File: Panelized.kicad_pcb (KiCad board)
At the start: 2 copper layers, 54.9 x 18.3 mm, 88 parts, among them J1 Conn_01x01_Pin, J2 Conn_01x01_Pin, J3 Conn_01x01_Pin, J4 Conn_01x01_Pin, Q1 AO3400A, Q2 AO3401A, U1 LM393

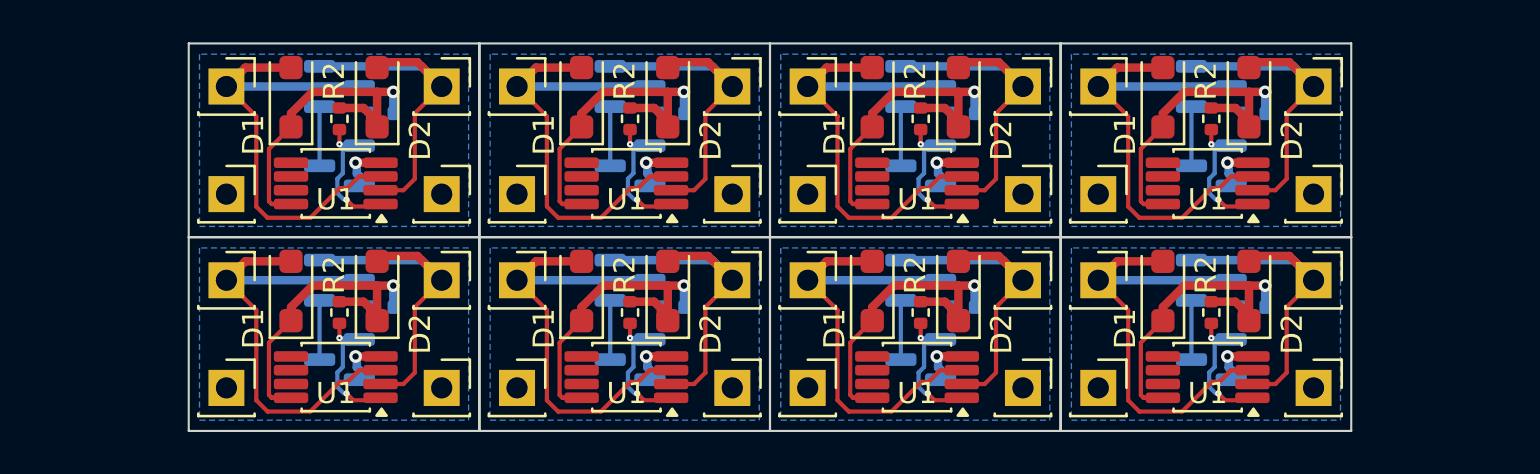
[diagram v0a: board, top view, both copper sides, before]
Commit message: Fixed wrong footprint issue
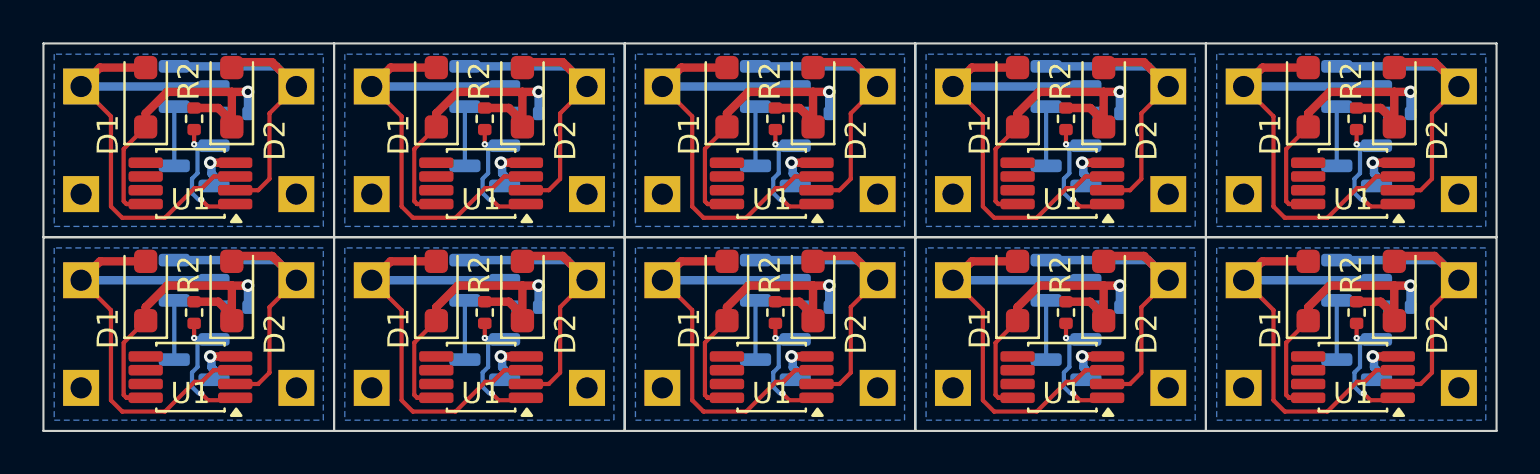
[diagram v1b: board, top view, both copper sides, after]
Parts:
- removed the D1 at (125.9, 31.7)
- removed the D1 at (139.6, 22.5)
- removed the D1 at (125.9, 22.5)
- removed the D1 at (167.0, 31.7)
- removed the D1 at (139.6, 31.7)
- removed the D1 at (167.0, 22.5)
- removed the D1 at (153.3, 22.5)
- removed the D1 at (153.3, 31.7)
- removed the D2 at (143.7, 31.7)
- removed the D2 at (171.1, 22.5)
- removed the D2 at (130.0, 31.7)
- removed the D2 at (157.4, 22.5)
- removed the D2 at (157.4, 31.7)
- removed the D2 at (130.0, 22.5)
- removed the D2 at (171.1, 31.7)
- removed the D2 at (143.7, 22.5)
- removed the J1 at (150.3, 22.0)
- removed the J1 at (164.0, 22.0)
- removed the J1 at (164.0, 31.2)
- removed the J1 at (122.8, 31.2)
- removed the J1 at (150.3, 31.2)
- removed the J1 at (136.6, 22.0)
- removed the J1 at (136.6, 31.2)
- removed the J1 at (122.8, 22.0)
- removed the J2 at (164.0, 27.1)
- removed the J2 at (150.3, 36.3)
- removed the J2 at (136.6, 27.1)
- removed the J2 at (150.3, 27.1)
- removed the J2 at (136.6, 36.3)
- removed the J2 at (122.8, 27.1)
- removed the J2 at (164.0, 36.3)
- removed the J2 at (122.8, 36.3)
- removed the J3 at (174.2, 31.2)
- removed the J3 at (174.2, 22.0)
- removed the J3 at (146.7, 22.0)
- removed the J3 at (133.0, 31.2)
- removed the J3 at (160.4, 31.2)
- removed the J3 at (146.7, 31.2)
- removed the J3 at (133.0, 22.0)
- removed the J3 at (160.4, 22.0)
- removed the J4 at (146.7, 27.1)
- removed the J4 at (160.4, 36.3)
- removed the J4 at (133.0, 27.1)
- removed the J4 at (133.0, 36.3)
- removed the J4 at (146.7, 36.3)
- removed the J4 at (174.2, 36.3)
- removed the J4 at (160.4, 27.1)
- removed the J4 at (174.2, 27.1)
- removed the Q1 at (128.2, 34.9)
- removed the Q1 at (128.2, 25.8)
- removed the Q1 at (155.6, 34.9)
- removed the Q1 at (169.3, 34.9)
- removed the Q1 at (141.9, 25.8)
- removed the Q1 at (155.6, 25.8)
- removed the Q1 at (141.9, 34.9)
- removed the Q1 at (169.3, 25.8)
- removed the Q2 at (169.3, 31.2)
- removed the Q2 at (155.6, 31.2)
- removed the Q2 at (141.9, 31.2)
- removed the Q2 at (128.2, 22.0)
- removed the Q2 at (169.3, 22.0)
- removed the Q2 at (141.9, 22.0)
- removed the Q2 at (155.6, 22.0)
- removed the Q2 at (128.2, 31.2)
- removed the R1 at (143.9, 23.3)
- removed the R1 at (157.6, 32.4)
- removed the R1 at (143.9, 32.4)
- removed the R1 at (130.2, 32.4)
- removed the R1 at (171.4, 32.4)
- removed the R1 at (130.2, 23.3)
- removed the R1 at (171.4, 23.3)
- removed the R1 at (157.6, 23.3)
- removed the R2 at (155.6, 32.7)
- removed the R2 at (128.2, 23.6)
- removed the R2 at (141.9, 32.7)
- removed the R2 at (169.3, 32.7)
- removed the R2 at (155.6, 23.6)
- removed the R2 at (169.3, 23.6)
- removed the R2 at (141.9, 23.6)
- removed the R2 at (128.2, 32.7)
- removed the U1 at (128.0, 35.7)
- removed the U1 at (141.7, 26.6)
- removed the U1 at (128.0, 26.6)
- removed the U1 at (169.2, 35.7)
- removed the U1 at (169.2, 26.6)
- removed the U1 at (155.4, 26.6)
- removed the U1 at (141.7, 35.7)
- removed the U1 at (155.4, 35.7)
- added D1: PMEG2020EH, Diode_SMD:D_SOD-123F, F.Cu at (160.2, 22.5)
- added D1: PMEG2020EH, Diode_SMD:D_SOD-123F, F.Cu at (119.0, 22.5)
- added D1: PMEG2020EH, Diode_SMD:D_SOD-123F, F.Cu at (146.5, 22.5)
- added D1: PMEG2020EH, Diode_SMD:D_SOD-123F, F.Cu at (173.9, 22.5)
- added D1: PMEG2020EH, Diode_SMD:D_SOD-123F, F.Cu at (173.9, 31.7)
- added D1: PMEG2020EH, Diode_SMD:D_SOD-123F, F.Cu at (132.8, 22.5)
- added D1: PMEG2020EH, Diode_SMD:D_SOD-123F, F.Cu at (146.5, 31.7)
- added D1: PMEG2020EH, Diode_SMD:D_SOD-123F, F.Cu at (132.8, 31.7)
- added D1: PMEG2020EH, Diode_SMD:D_SOD-123F, F.Cu at (119.0, 31.7)
- added D1: PMEG2020EH, Diode_SMD:D_SOD-123F, F.Cu at (160.2, 31.7)
- added D2: PMEG2020EH, Diode_SMD:D_SOD-123F, F.Cu at (178.0, 22.5)
- added D2: PMEG2020EH, Diode_SMD:D_SOD-123F, F.Cu at (150.5, 22.5)
- added D2: PMEG2020EH, Diode_SMD:D_SOD-123F, F.Cu at (178.0, 31.7)
- added D2: PMEG2020EH, Diode_SMD:D_SOD-123F, F.Cu at (136.8, 22.5)
- added D2: PMEG2020EH, Diode_SMD:D_SOD-123F, F.Cu at (164.2, 22.5)
- added D2: PMEG2020EH, Diode_SMD:D_SOD-123F, F.Cu at (136.8, 31.7)
- added D2: PMEG2020EH, Diode_SMD:D_SOD-123F, F.Cu at (150.5, 31.7)
- added D2: PMEG2020EH, Diode_SMD:D_SOD-123F, F.Cu at (123.1, 22.5)
- added D2: PMEG2020EH, Diode_SMD:D_SOD-123F, F.Cu at (164.2, 31.7)
- added D2: PMEG2020EH, Diode_SMD:D_SOD-123F, F.Cu at (123.1, 31.7)
- added J1: Conn_01x01_Pin, Connector_PinHeader_2.54mm:PinHeader_1x01_P2.54mm_Vertical, B.Cu at (170.9, 22.0)
- added J1: Conn_01x01_Pin, Connector_PinHeader_2.54mm:PinHeader_1x01_P2.54mm_Vertical, B.Cu at (157.1, 31.2)
- added J1: Conn_01x01_Pin, Connector_PinHeader_2.54mm:PinHeader_1x01_P2.54mm_Vertical, B.Cu at (116.0, 22.0)
- added J1: Conn_01x01_Pin, Connector_PinHeader_2.54mm:PinHeader_1x01_P2.54mm_Vertical, B.Cu at (157.1, 22.0)
- added J1: Conn_01x01_Pin, Connector_PinHeader_2.54mm:PinHeader_1x01_P2.54mm_Vertical, B.Cu at (129.7, 22.0)
- added J1: Conn_01x01_Pin, Connector_PinHeader_2.54mm:PinHeader_1x01_P2.54mm_Vertical, B.Cu at (129.7, 31.2)
- added J1: Conn_01x01_Pin, Connector_PinHeader_2.54mm:PinHeader_1x01_P2.54mm_Vertical, B.Cu at (143.4, 22.0)
- added J1: Conn_01x01_Pin, Connector_PinHeader_2.54mm:PinHeader_1x01_P2.54mm_Vertical, B.Cu at (116.0, 31.2)
- added J1: Conn_01x01_Pin, Connector_PinHeader_2.54mm:PinHeader_1x01_P2.54mm_Vertical, B.Cu at (143.4, 31.2)
- added J1: Conn_01x01_Pin, Connector_PinHeader_2.54mm:PinHeader_1x01_P2.54mm_Vertical, B.Cu at (170.9, 31.2)
- added J2: Conn_01x01_Pin, Connector_PinHeader_2.54mm:PinHeader_1x01_P2.54mm_Vertical, B.Cu at (129.7, 27.1)
- added J2: Conn_01x01_Pin, Connector_PinHeader_2.54mm:PinHeader_1x01_P2.54mm_Vertical, B.Cu at (157.1, 36.3)
- added J2: Conn_01x01_Pin, Connector_PinHeader_2.54mm:PinHeader_1x01_P2.54mm_Vertical, B.Cu at (143.4, 27.1)
- added J2: Conn_01x01_Pin, Connector_PinHeader_2.54mm:PinHeader_1x01_P2.54mm_Vertical, B.Cu at (157.1, 27.1)
- added J2: Conn_01x01_Pin, Connector_PinHeader_2.54mm:PinHeader_1x01_P2.54mm_Vertical, B.Cu at (116.0, 36.3)
- added J2: Conn_01x01_Pin, Connector_PinHeader_2.54mm:PinHeader_1x01_P2.54mm_Vertical, B.Cu at (116.0, 27.1)
- added J2: Conn_01x01_Pin, Connector_PinHeader_2.54mm:PinHeader_1x01_P2.54mm_Vertical, B.Cu at (143.4, 36.3)
- added J2: Conn_01x01_Pin, Connector_PinHeader_2.54mm:PinHeader_1x01_P2.54mm_Vertical, B.Cu at (129.7, 36.3)
- added J2: Conn_01x01_Pin, Connector_PinHeader_2.54mm:PinHeader_1x01_P2.54mm_Vertical, B.Cu at (170.9, 36.3)
- added J2: Conn_01x01_Pin, Connector_PinHeader_2.54mm:PinHeader_1x01_P2.54mm_Vertical, B.Cu at (170.9, 27.1)
- added J3: Conn_01x01_Pin, Connector_PinHeader_2.54mm:PinHeader_1x01_P2.54mm_Vertical, B.Cu at (139.9, 22.0)
- added J3: Conn_01x01_Pin, Connector_PinHeader_2.54mm:PinHeader_1x01_P2.54mm_Vertical, B.Cu at (181.0, 22.0)
- added J3: Conn_01x01_Pin, Connector_PinHeader_2.54mm:PinHeader_1x01_P2.54mm_Vertical, B.Cu at (167.3, 22.0)
- added J3: Conn_01x01_Pin, Connector_PinHeader_2.54mm:PinHeader_1x01_P2.54mm_Vertical, B.Cu at (167.3, 31.2)
- added J3: Conn_01x01_Pin, Connector_PinHeader_2.54mm:PinHeader_1x01_P2.54mm_Vertical, B.Cu at (153.6, 22.0)
- added J3: Conn_01x01_Pin, Connector_PinHeader_2.54mm:PinHeader_1x01_P2.54mm_Vertical, B.Cu at (153.6, 31.2)
- added J3: Conn_01x01_Pin, Connector_PinHeader_2.54mm:PinHeader_1x01_P2.54mm_Vertical, B.Cu at (126.1, 31.2)
- added J3: Conn_01x01_Pin, Connector_PinHeader_2.54mm:PinHeader_1x01_P2.54mm_Vertical, B.Cu at (181.0, 31.2)
- added J3: Conn_01x01_Pin, Connector_PinHeader_2.54mm:PinHeader_1x01_P2.54mm_Vertical, B.Cu at (139.9, 31.2)
- added J3: Conn_01x01_Pin, Connector_PinHeader_2.54mm:PinHeader_1x01_P2.54mm_Vertical, B.Cu at (126.1, 22.0)
- added J4: Conn_01x01_Pin, Connector_PinHeader_2.54mm:PinHeader_1x01_P2.54mm_Vertical, B.Cu at (181.0, 27.1)
- added J4: Conn_01x01_Pin, Connector_PinHeader_2.54mm:PinHeader_1x01_P2.54mm_Vertical, B.Cu at (153.6, 27.1)
- added J4: Conn_01x01_Pin, Connector_PinHeader_2.54mm:PinHeader_1x01_P2.54mm_Vertical, B.Cu at (126.1, 27.1)
- added J4: Conn_01x01_Pin, Connector_PinHeader_2.54mm:PinHeader_1x01_P2.54mm_Vertical, B.Cu at (139.9, 27.1)
- added J4: Conn_01x01_Pin, Connector_PinHeader_2.54mm:PinHeader_1x01_P2.54mm_Vertical, B.Cu at (181.0, 36.3)
- added J4: Conn_01x01_Pin, Connector_PinHeader_2.54mm:PinHeader_1x01_P2.54mm_Vertical, B.Cu at (139.9, 36.3)
- added J4: Conn_01x01_Pin, Connector_PinHeader_2.54mm:PinHeader_1x01_P2.54mm_Vertical, B.Cu at (126.1, 36.3)
- added J4: Conn_01x01_Pin, Connector_PinHeader_2.54mm:PinHeader_1x01_P2.54mm_Vertical, B.Cu at (153.6, 36.3)
- added J4: Conn_01x01_Pin, Connector_PinHeader_2.54mm:PinHeader_1x01_P2.54mm_Vertical, B.Cu at (167.3, 36.3)
- added J4: Conn_01x01_Pin, Connector_PinHeader_2.54mm:PinHeader_1x01_P2.54mm_Vertical, B.Cu at (167.3, 27.1)
- added Q1: AO3400A, Package_TO_SOT_SMD:SOT-23, B.Cu at (121.3, 34.9)
- added Q1: AO3400A, Package_TO_SOT_SMD:SOT-23, B.Cu at (121.3, 25.8)
- added Q1: AO3400A, Package_TO_SOT_SMD:SOT-23, B.Cu at (162.5, 25.8)
- added Q1: AO3400A, Package_TO_SOT_SMD:SOT-23, B.Cu at (135.0, 25.8)
- added Q1: AO3400A, Package_TO_SOT_SMD:SOT-23, B.Cu at (176.2, 34.9)
- added Q1: AO3400A, Package_TO_SOT_SMD:SOT-23, B.Cu at (148.8, 34.9)
- added Q1: AO3400A, Package_TO_SOT_SMD:SOT-23, B.Cu at (162.5, 34.9)
- added Q1: AO3400A, Package_TO_SOT_SMD:SOT-23, B.Cu at (135.0, 34.9)
- added Q1: AO3400A, Package_TO_SOT_SMD:SOT-23, B.Cu at (148.8, 25.8)
- added Q1: AO3400A, Package_TO_SOT_SMD:SOT-23, B.Cu at (176.2, 25.8)
- added Q2: AO3401A, Package_TO_SOT_SMD:SOT-23, B.Cu at (148.8, 22.0)
- added Q2: AO3401A, Package_TO_SOT_SMD:SOT-23, B.Cu at (135.0, 22.0)
- added Q2: AO3401A, Package_TO_SOT_SMD:SOT-23, B.Cu at (121.3, 22.0)
- added Q2: AO3401A, Package_TO_SOT_SMD:SOT-23, B.Cu at (121.3, 31.2)
- added Q2: AO3401A, Package_TO_SOT_SMD:SOT-23, B.Cu at (162.5, 22.0)
- added Q2: AO3401A, Package_TO_SOT_SMD:SOT-23, B.Cu at (176.2, 22.0)
- added Q2: AO3401A, Package_TO_SOT_SMD:SOT-23, B.Cu at (135.0, 31.2)
- added Q2: AO3401A, Package_TO_SOT_SMD:SOT-23, B.Cu at (148.8, 31.2)
- added Q2: AO3401A, Package_TO_SOT_SMD:SOT-23, B.Cu at (176.2, 31.2)
- added Q2: AO3401A, Package_TO_SOT_SMD:SOT-23, B.Cu at (162.5, 31.2)
- added R1: 10k, Resistor_SMD:R_0402_1005Metric, B.Cu at (178.2, 23.3)
- added R1: 10k, Resistor_SMD:R_0402_1005Metric, B.Cu at (137.1, 23.3)
- added R1: 10k, Resistor_SMD:R_0402_1005Metric, B.Cu at (123.4, 32.4)
- added R1: 10k, Resistor_SMD:R_0402_1005Metric, B.Cu at (164.5, 23.3)
- added R1: 10k, Resistor_SMD:R_0402_1005Metric, B.Cu at (178.2, 32.4)
- added R1: 10k, Resistor_SMD:R_0402_1005Metric, B.Cu at (164.5, 32.4)
- added R1: 10k, Resistor_SMD:R_0402_1005Metric, B.Cu at (150.8, 32.4)
- added R1: 10k, Resistor_SMD:R_0402_1005Metric, B.Cu at (137.1, 32.4)
- added R1: 10k, Resistor_SMD:R_0402_1005Metric, B.Cu at (150.8, 23.3)
- added R1: 10k, Resistor_SMD:R_0402_1005Metric, B.Cu at (123.4, 23.3)
- added R2: 10k, Resistor_SMD:R_0402_1005Metric, F.Cu at (162.5, 23.6)
- added R2: 10k, Resistor_SMD:R_0402_1005Metric, F.Cu at (148.8, 23.6)
- added R2: 10k, Resistor_SMD:R_0402_1005Metric, F.Cu at (162.5, 32.7)
- added R2: 10k, Resistor_SMD:R_0402_1005Metric, F.Cu at (135.0, 23.6)
- added R2: 10k, Resistor_SMD:R_0402_1005Metric, F.Cu at (176.2, 23.6)
- added R2: 10k, Resistor_SMD:R_0402_1005Metric, F.Cu at (135.0, 32.7)
- added R2: 10k, Resistor_SMD:R_0402_1005Metric, F.Cu at (121.3, 23.6)
- added R2: 10k, Resistor_SMD:R_0402_1005Metric, F.Cu at (148.8, 32.7)
- added R2: 10k, Resistor_SMD:R_0402_1005Metric, F.Cu at (176.2, 32.7)
- added R2: 10k, Resistor_SMD:R_0402_1005Metric, F.Cu at (121.3, 32.7)
- added U1: LM393, Package_SO:VSSOP-8_3x3mm_P0.65mm, F.Cu at (134.9, 35.7)
- added U1: LM393, Package_SO:VSSOP-8_3x3mm_P0.65mm, F.Cu at (121.1, 35.7)
- added U1: LM393, Package_SO:VSSOP-8_3x3mm_P0.65mm, F.Cu at (176.0, 35.7)
- added U1: LM393, Package_SO:VSSOP-8_3x3mm_P0.65mm, F.Cu at (148.6, 35.7)
- added U1: LM393, Package_SO:VSSOP-8_3x3mm_P0.65mm, F.Cu at (162.3, 35.7)
- added U1: LM393, Package_SO:VSSOP-8_3x3mm_P0.65mm, F.Cu at (176.0, 26.6)
- added U1: LM393, Package_SO:VSSOP-8_3x3mm_P0.65mm, F.Cu at (162.3, 26.6)
- added U1: LM393, Package_SO:VSSOP-8_3x3mm_P0.65mm, F.Cu at (121.1, 26.6)
- added U1: LM393, Package_SO:VSSOP-8_3x3mm_P0.65mm, F.Cu at (148.6, 26.6)
- added U1: LM393, Package_SO:VSSOP-8_3x3mm_P0.65mm, F.Cu at (134.9, 26.6)
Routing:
- net Board_9-/i: track 0.00 -> 23.4 mm
- net Board_8-/i: track 0.00 -> 23.4 mm
- net Board_9-/o: track 0.00 -> 16.4 mm
- net Board_8-/o: track 0.00 -> 16.4 mm
- net Board_9-/a: track 0.00 -> 15.6 mm, vias 0 -> 1
- net Board_8-/a: track 0.00 -> 15.6 mm, vias 0 -> 1
- net Board_8-Net-(Q1-G): track 0.00 -> 6.36 mm, vias 0 -> 2
- net Board_9-Net-(Q1-G): track 0.00 -> 6.36 mm, vias 0 -> 2
- net Board_8-Net-(Q1-D): track 0.00 -> 5.39 mm
- net Board_9-Net-(Q1-D): track 0.00 -> 5.39 mm
- net Board_9-GND: track 0.00 -> 2.35 mm, vias 0 -> 1
- net Board_8-GND: track 0.00 -> 2.35 mm, vias 0 -> 1
- added copper zone on B.Cu, net Board_8-GND
- added copper zone on B.Cu, net Board_9-GND
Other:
- board size 54.9 x 18.3 mm -> 68.6 x 18.3 mm
